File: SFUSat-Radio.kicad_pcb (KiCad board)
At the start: 4 copper layers, 95.9 x 90.2 mm, 282 parts, among them J1 PC104-8BIT, J10 TP_TH_150, J11 TP_TH_150, J12 SMA, J13 SMA, J14 SMA, J15 Conn_01x02, J16 SMA, J17 SMA, J18 SMA, J2 PC104PTH, J21 TP_TH_150, J22 TP_TH_150, J23 TP_TH_150, J24 TP_TH_150, J25 Conn_01x02, J3 PC104PTH, J4 PC104PTH, J400 SMA, J401 TP_TH_150, J402 TP_TH_150, J404 TP_TH_150, J405 TP_TH_150, J406 TP_TH_150, J5 PC104PTH, J500 SMA, J501 TP_TH_150, J502 TP_TH_150, J504 TP_TH_150, J505 TP_TH_150, J506 TP_TH_150, J6 SMA, J7 TP_TH_150, J8 TP_TH_150, J9 TP_TH_150, P1 3pin-DC-power, U1 SINGLE_0402, U10 TPS799, U100 CC1101-Q1, U101 0433BM15A0001, U11 SINGLE_0402, U110 CC1101-Q1, U111 0915BM15A0001E, U12 CONN_02X05_SHRD, U13 CONN_02X05_SHRD, U14 2N7002DW, U15 TPS62175DQCR, U16 TPS71750DSER, U17 74LVC1G14SE-7, U2 SKY13345-368LF, U3 CD4555BPWR, U4 LMS3635AQRNLRQ1, U400 SINGLE_0402, U401 LMV358, U402 RF6886, U420 2N7002DW, U5 MML09211H, U500 SINGLE_0402, U501 LMV358, U502 RF6886, U6 SINGLE_0402, U600 STLM75, U610 STLM75, U7 SKY13372-467LF, U8 SINGLE_0402, U9 TLV702, X100 NX3225GA, X110 NX3225GA

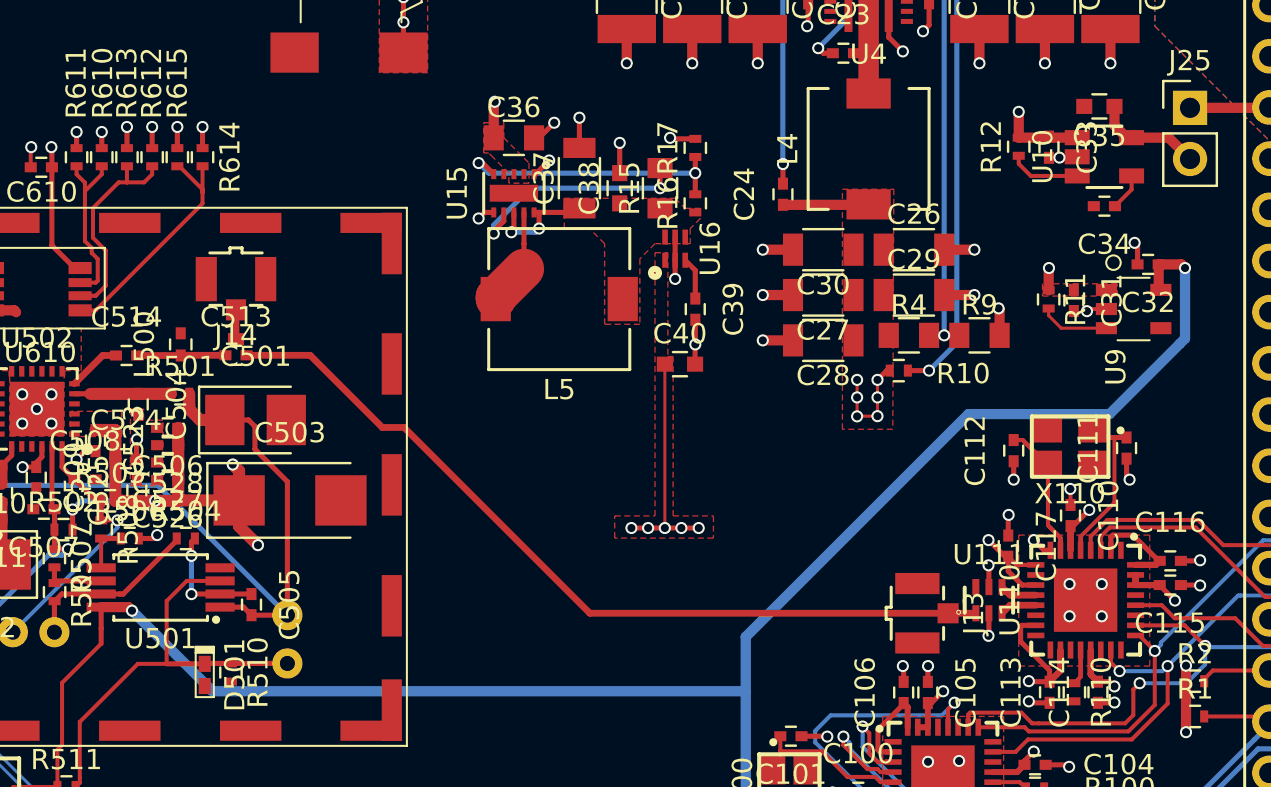
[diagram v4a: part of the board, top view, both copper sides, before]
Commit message: changed clearance of all planes to 0.2mm. 0.1524mm is too close to PCBway's manufacturable limit
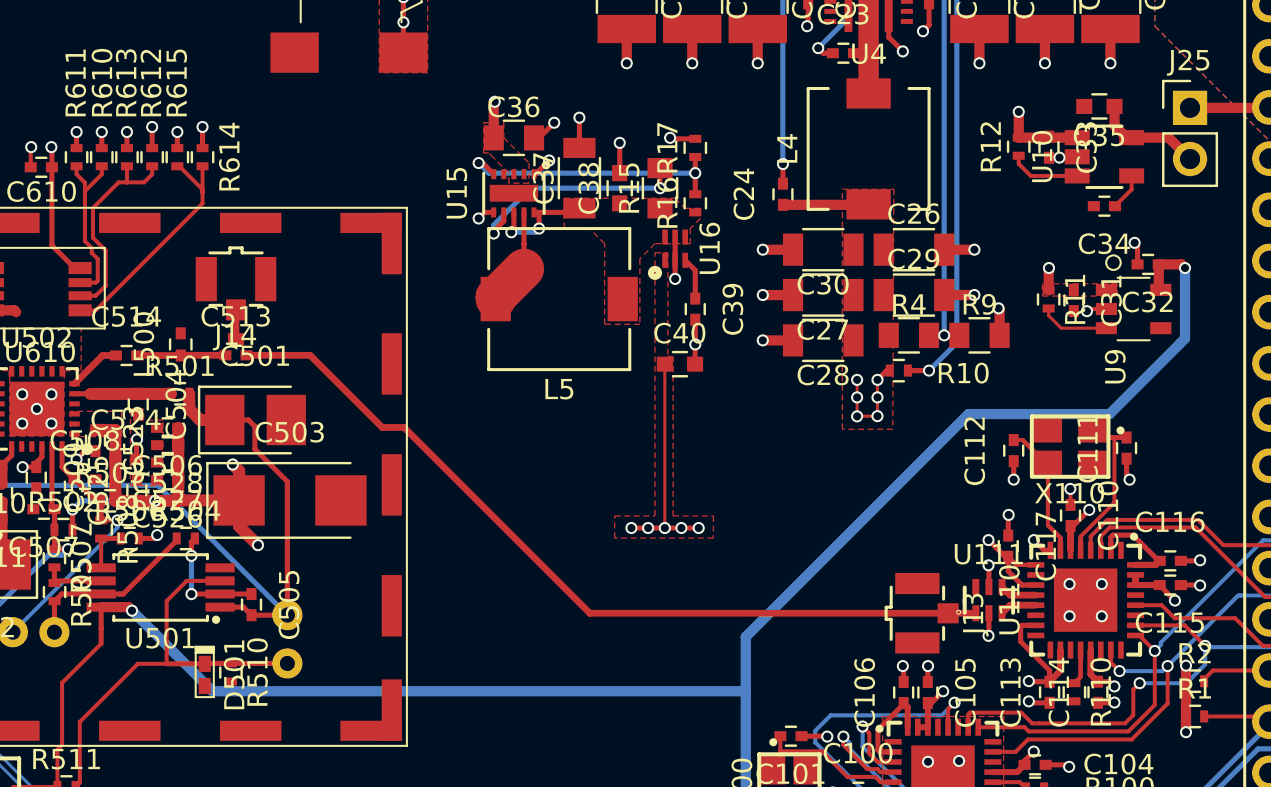
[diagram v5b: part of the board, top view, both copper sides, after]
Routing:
- net GND: track 120.1 -> 124.1 mm
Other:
- net class Power: clearance 0.2 -> 0.1524
- net class VCC removed
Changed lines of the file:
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@@
     (thickness 1.6)
     (drawings 26)
-    (tracks 1611)
+    (tracks 1615)
     (zones 0)
     (modules 282)
@@
   )
   (setup
-    (last_trace_width 0.508)
+    (last_trace_width 0.254)
     (user_trace_width 0.1524)
     (user_trace_width 0.2)
@@
     (user_trace_width 2)
     (trace_clearance 0.1524)
-    (zone_clearance 0.154)
+    (zone_clearance 0.2)
     (zone_45_only yes)
     (trace_min 0.1524)
@@
   )
   (net_class Power ""
-    (clearance 0.2)
+    (clearance 0.1524)
     (trace_width 0.254)
     (via_dia 0.6)
@@
     (add_net "Net-(J6-Pad1)")
   )
-  (net_class VCC ""
-    (clearance 0.2)
-    (trace_width 0.2)
-    (via_dia 0.6)
-    (via_drill 0.4)
-    (uvia_dia 0.3)
-    (uvia_drill 0.1)
-  )
   (module SFUSat:CC1101-Q1 (layer F.Cu)
     (at 179.49 104.26)
@@
     (pad 2 thru_hole oval (at 0 2.54) (size 1.7 1.7) (drill 1) (layers *.Cu *.Mask)
       (net 197 "/3.3V Regulator/3V3OUT"))
-    (model ${KISYS3DMOD}/Socket_Strips.3dshapes/Socket_Strip_Straight_1x02_Pitch2.54mm.wrl
+    (model ../../../../../home/tobi/Cubesat/CubeSat-Radio/KiCad-Lib/SFUSat.pretty/2.54mm_Jumper.wrl
       (at (xyz 0 -0.05 0))
       (scale (xyz 1 1 1))
@@
   (gr_line (start 112.5 58.33) (end 208.39 58.33) (angle 90) (layer Edge.Cuts) (width 0.1))
   (gr_line (start 112.5 148.5) (end 208.39 148.5) (angle 90) (layer Edge.Cuts) (width 0.1))
+  (segment (start 186.57 95.48) (end 185.77 94.68) (width 0.254) (layer F.Cu) (net 1))
+  (segment (start 186.57 95.48) (end 187.37 96.28) (width 0.254) (layer F.Cu) (net 1))
+  (segment (start 186.57 95.48) (end 187.37 94.68) (width 0.254) (layer F.Cu) (net 1))
+  (segment (start 186.57 95.48) (end 185.77 96.28) (width 0.254) (layer F.Cu) (net 1))
+  (segment (start 159.5 118.3) (end 159.5 117.5) (width 0.254) (layer F.Cu) (net 1))
+  (via (at 159.5 117.5) (size 0.6) (drill 0.4) (layers F.Cu B.Cu) (net 1))
+  (segment (start 141.5 73.05) (end 141.5 72.25) (width 0.254) (layer F.Cu) (net 1))
+  (via (at 141.5 72.25) (size 0.6) (drill 0.4) (layers F.Cu B.Cu) (net 1))
+  (segment (start 139 73.05) (end 139 72.25) (width 0.254) (layer F.Cu) (net 1))
+  (via (at 139 72.25) (size 0.6) (drill 0.4) (layers F.Cu B.Cu) (net 1))
   (segment (start 174.765 105.01) (end 174.03 105.01) (width 0.2) (layer F.Cu) (net 1))
   (segment (start 174.03 105.01) (end 174.02 105.02) (width 0.2) (layer F.Cu) (net 1))
@@
   (segment (start 150.497844 125.695) (end 150.497844 126.747844) (width 0.508) (layer F.Cu) (net 1))
   (segment (start 150.497844 126.747844) (end 150.5 126.75) (width 0.508) (layer F.Cu) (net 1))
-  (segment (start 159.5 118.3) (end 159.5 117.5) (width 0.254) (layer F.Cu) (net 1))
   (segment (start 150.497844 125.695) (end 152.195 125.695) (width 0.508) (layer F.Cu) (net 1))
   (segment (start 152.195 125.695) (end 152.25 125.75) (width 0.508) (layer F.Cu) (net 1))
@@
   (segment (start 152.225 118.025) (end 152.25 118) (width 0.2) (layer F.Cu) (net 1))
   (via (at 152.25 118) (size 0.6) (drill 0.4) (layers F.Cu B.Cu) (net 1))
-  (segment (start 141.5 73.05) (end 141.5 72) (width 0.254) (layer F.Cu) (net 1))
-  (via (at 141.5 72) (size 0.6) (drill 0.4) (layers F.Cu B.Cu) (net 1))
-  (segment (start 139 73.05) (end 139 72) (width 0.254) (layer F.Cu) (net 1))
-  (via (at 139 72) (size 0.6) (drill 0.4) (layers F.Cu B.Cu) (net 1))
   (segment (start 136.5 73.05) (end 136.5 72.25) (width 0.254) (layer F.Cu) (net 1))
   (via (at 136.5 72.25) (size 0.6) (drill 0.4) (layers F.Cu B.Cu) (net 1))
-  (via (at 159.5 117.5) (size 0.6) (drill 0.4) (layers F.Cu B.Cu) (net 1))
   (segment (start 157 118.3) (end 157 117.5) (width 0.254) (layer F.Cu) (net 1))
   (via (at 157 117.5) (size 0.6) (drill 0.4) (layers F.Cu B.Cu) (net 1))
@@
   )
   (zone (net 1) (net_name GND) (layer B.Cu) (hatch full 0.508)
-    (connect_pads yes (clearance 0.1524))
+    (connect_pads yes (clearance 0.2))
     (min_thickness 0.0254)
     (fill yes (arc_segments 16) (thermal_gap 0.127) (thermal_bridge_width 0.127))
@@
   )
   (zone (net 1) (net_name GND) (layer GND.Cu) (hatch full 0.508)
-    (connect_pads (clearance 0.1524))
+    (connect_pads (clearance 0.2))
     (min_thickness 0.254)
     (fill yes (arc_segments 16) (thermal_gap 0.127) (thermal_bridge_width 0.26))
@@
   )
   (zone (net 66) (net_name /3V3) (layer PWR.Cu) (hatch full 0.508)
-    (connect_pads (clearance 0.1524))
+    (connect_pads (clearance 0.2))
     (min_thickness 0.254)
     (fill yes (arc_segments 16) (thermal_gap 0.127) (thermal_bridge_width 0.26))
@@
     (polygon
       (pts
-        (xy 191.75 69.25) (xy 181.5 69.25) (xy 181.5 80.5) (xy 183 80.5) (xy 183 84.25)
-        (xy 183.5 84.25) (xy 183.5 80) (xy 182 80) (xy 182 69.75) (xy 191.75 69.75)
+        (xy 191.75 69.25) (xy 181.5 69.25) (xy 181.5 80.5) (xy 181.5 84.25) (xy 181.75 84.25)
+        (xy 181.75 80) (xy 181.75 69.75) (xy 191.75 69.75)
       )
     )
@@
   (zone (net 181) (net_name /VIN) (layer PWR.Cu) (hatch edge 0.508)
     (priority 1)
-    (connect_pads yes (clearance 0.1524))
+    (connect_pads yes (clearance 0.2))
     (min_thickness 0.254)
     (fill yes (arc_segments 16) (thermal_gap 0.508) (thermal_bridge_width 0.508))
     (polygon
       (pts
-        (xy 192.75 69.25) (xy 169.5 69.25) (xy 169.5 69.75) (xy 169.5 84.25) (xy 155.75 84.25)
-        (xy 155.76 69.33) (xy 151.52 69.32) (xy 151.52 58.23) (xy 192.5 58.25) (xy 192.75 58.25)
+        (xy 192.75 69.25) (xy 181.5 69.25) (xy 181.5 84.25) (xy 155.75 84.25) (xy 155.76 69.33)
+        (xy 151.52 69.32) (xy 151.52 58.23) (xy 192.5 58.25) (xy 192.75 58.25)
       )
     )
   )
   (zone (net 76) (net_name /3V6) (layer PWR.Cu) (hatch full 0.508)
-    (priority 1)
-    (connect_pads yes (clearance 0.1524))
+    (priority 2)
+    (connect_pads yes (clearance 0.2))
     (min_thickness 0.254)
     (fill yes (arc_segments 16) (thermal_gap 0.127) (thermal_bridge_width 0.26))
     (polygon
       (pts
-        (xy 182 69.75) (xy 182 80) (xy 183.5 80) (xy 183.5 84.2) (xy 155.8 84.2)
-        (xy 155.8 76) (xy 114 76) (xy 114 103) (xy 131.6 103) (xy 131.6 142.2)
-        (xy 170.6 142.2) (xy 170.6 121) (xy 147.5 121) (xy 147.5 106.25) (xy 153 106.25)
-        (xy 153 90.9) (xy 182.5 90.9) (xy 182.5 86) (xy 187.75 86) (xy 187.75 69.75)
+        (xy 181.75 69.75) (xy 181.75 80) (xy 181.75 84.25) (xy 155.75 84.25) (xy 155.75 76)
+        (xy 114 76) (xy 114 103) (xy 131.6 103) (xy 131.6 142.2) (xy 170.6 142.2)
+        (xy 170.6 121) (xy 147.5 121) (xy 147.5 106.25) (xy 153.5 106.25) (xy 153.5 90.9)
+        (xy 182.5 90.9) (xy 182.5 86) (xy 187.75 86) (xy 187.75 69.75)
       )
     )
@@
   (zone (net 115) (net_name /5V0) (layer PWR.Cu) (hatch edge 0.508)
     (priority 1)
-    (connect_pads yes (clearance 0.1524))
+    (connect_pads yes (clearance 0.2))
     (min_thickness 0.254)
     (fill yes (arc_segments 16) (thermal_gap 0.508) (thermal_bridge_width 0.508))
@@
       )
     )
-  )
-  (zone (net 1) (net_name GND) (layer F.Cu) (hatch full 0.508)
-    (connect_pads yes (clearance 0.2))
-    (min_thickness 0.2)
-    (fill yes (arc_segments 16) (thermal_gap 0.127) (thermal_bridge_width 0.26))
-    (polygon
-      (pts
-        (xy 183.25 92.25) (xy 189.75 92.25) (xy 189.75 98.75) (xy 183.25 98.75)
-      )
-    )
